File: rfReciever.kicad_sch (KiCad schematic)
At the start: 41 parts, among them J1 MOLEX 1054440001, J2 Conn_01x02, J3 Conn_01x02, J4 Conn_01x03, SW1 RF_RESET, SW2 RF_SLEEP, U1 TLV70130DBVR, U2 USBLC6-2SC6, U3 FT234XD-R, X1 DigiXBeeRX900Micro

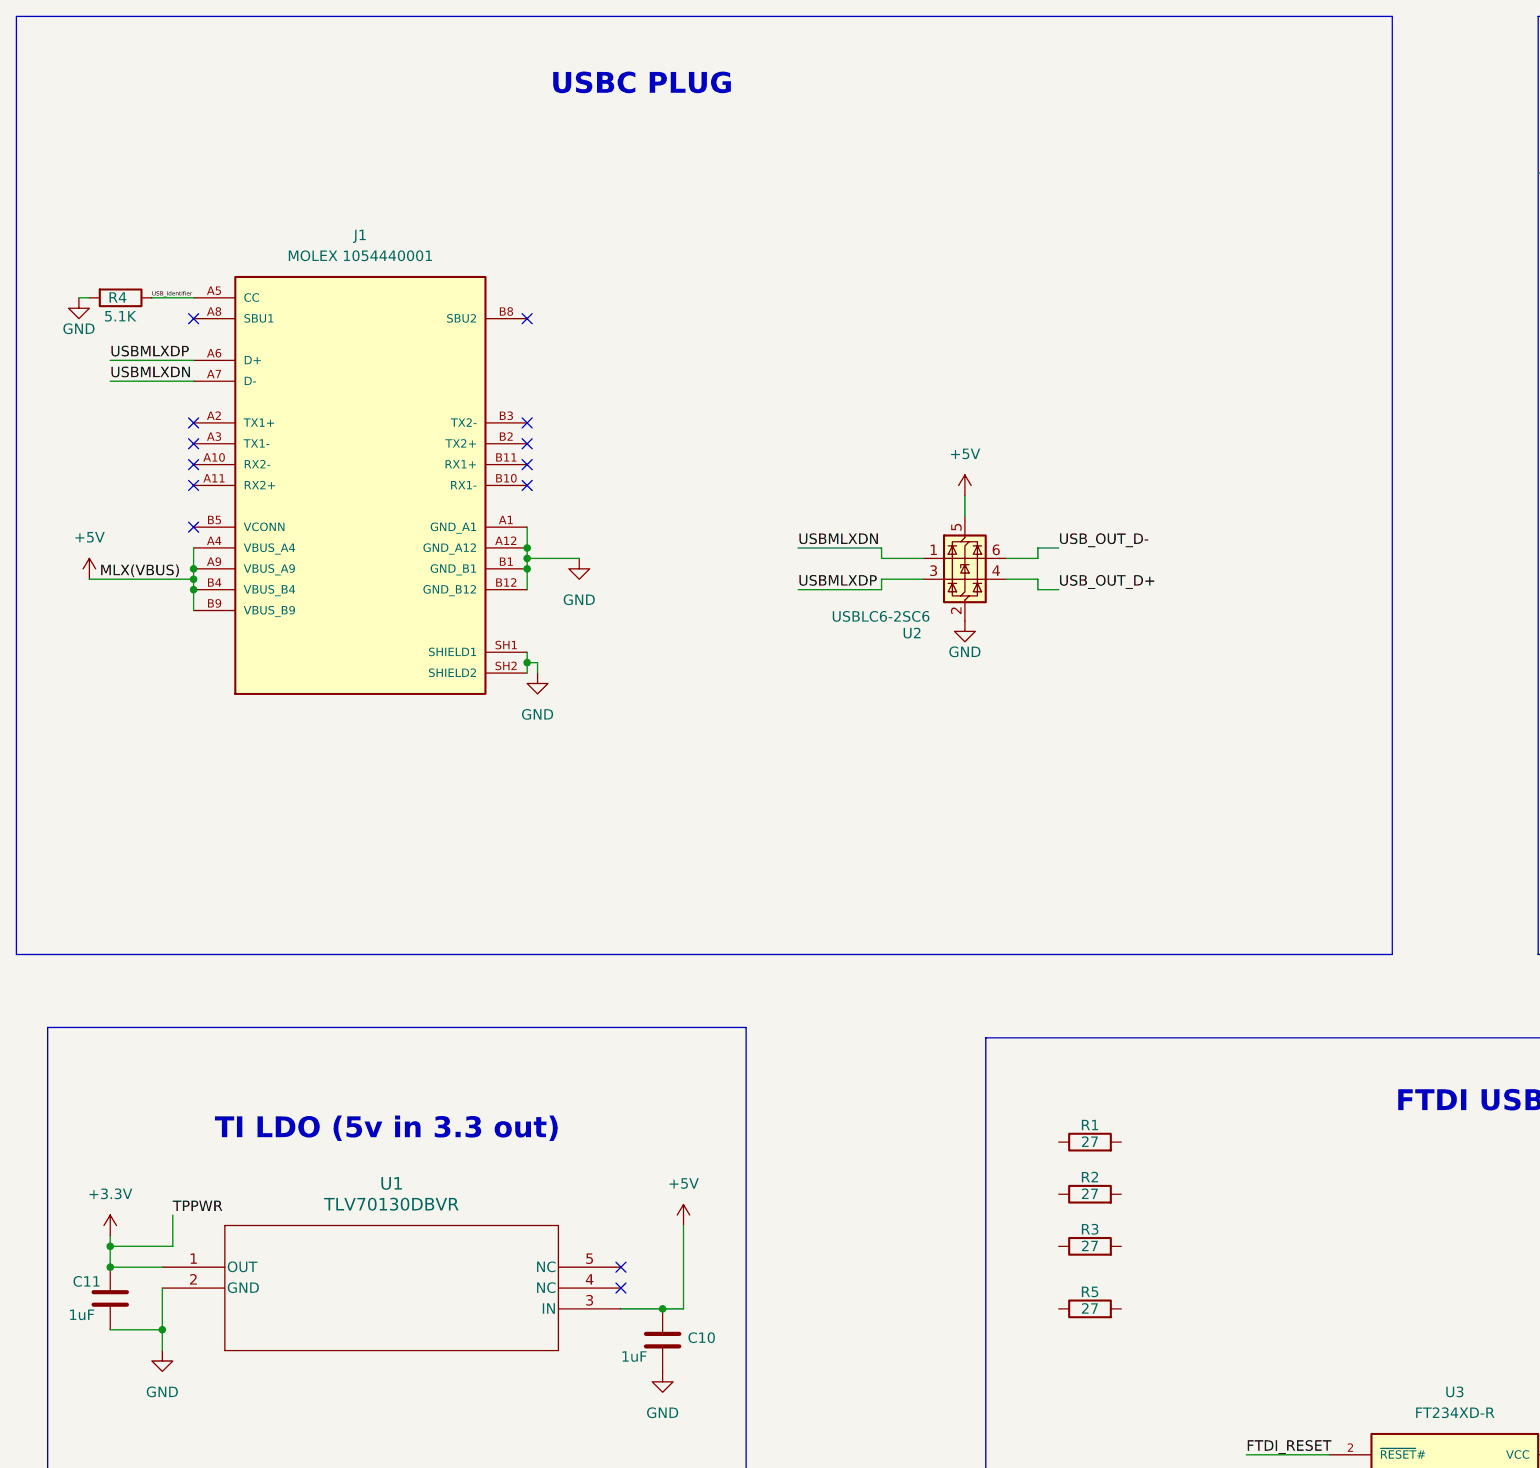
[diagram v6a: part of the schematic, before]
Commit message: More minor tweaks + silkscreen
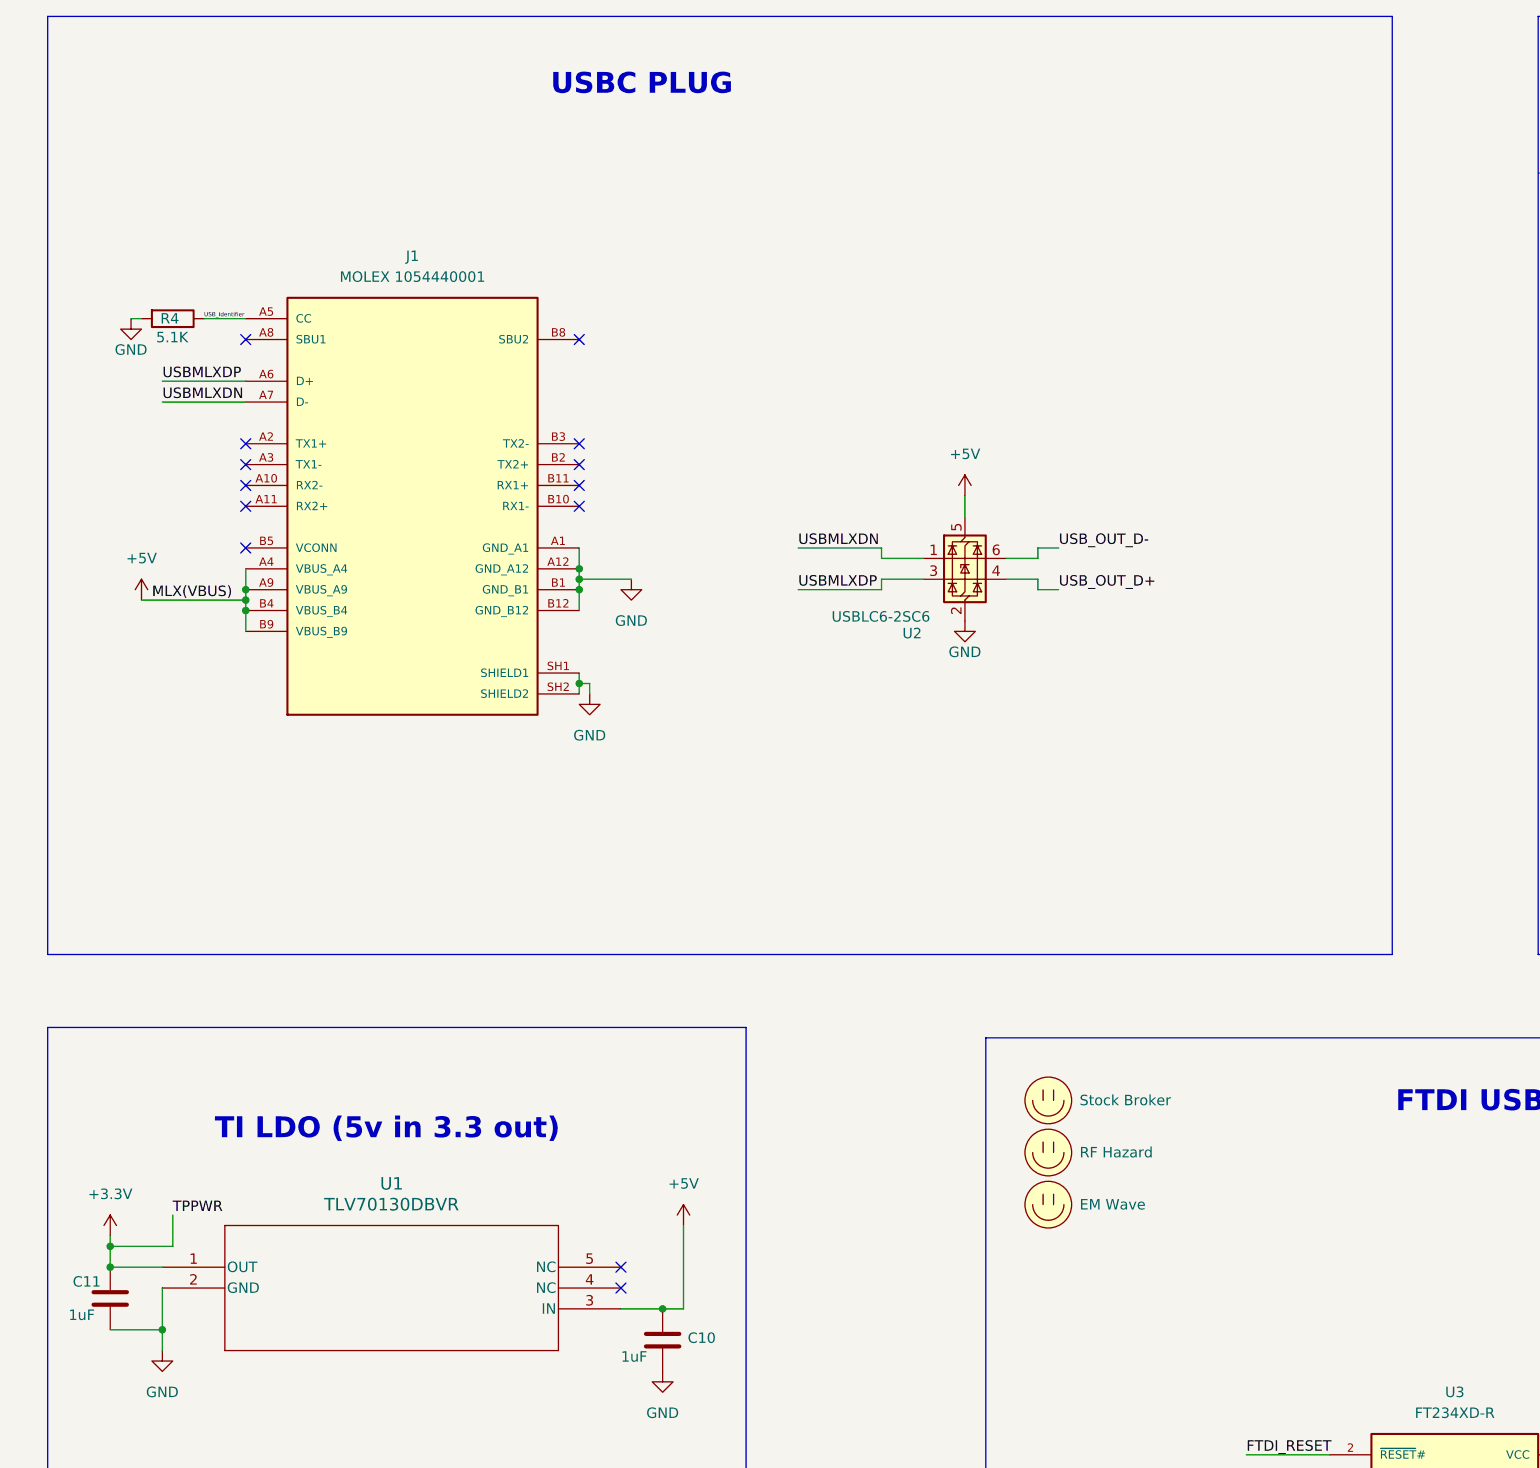
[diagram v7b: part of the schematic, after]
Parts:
- removed R1: 27, rfReciever-Footprints:stockBroker, symbol Device:R
- removed R2: 27, rfReciever-Footprints:RFHazard, symbol Device:R
- removed R3: 27, rfReciever-Footprints:dataNetwork, symbol Device:R
- removed R5: 27, rfReciever-Footprints:emWave, symbol Device:R
- added LOGO1: Stock Broker, rfReciever-Footprints:stockBroker, symbol utsvt-misc:Logo_Placeholder
- added LOGO2: RF Hazard, rfReciever-Footprints:RFHazard, symbol utsvt-misc:Logo_Placeholder
- added LOGO3: EM Wave, rfReciever-Footprints:emWave, symbol utsvt-misc:Logo_Placeholder
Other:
- moved on the sheet: J1, R4

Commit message: fixed drc
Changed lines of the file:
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@@
 (kicad_sch
-	(version 20231120)
+	(version 20250114)
 	(generator "eeschema")
-	(generator_version "8.0")
+	(generator_version "9.0")
 	(paper "A3")
+	(rectangle
+		(start 203.2 30.48)
+		(end 370.84 144.78)
+		(stroke
+			(width 0)
+			(type default)
+		)
+		(fill
+			(type none)
+		)
+	)
+	(rectangle
+		(start 299.72 167.64)
+		(end 382.27 213.36)
+		(stroke
+			(width 0)
+			(type default)
+		)
+		(fill
+			(type none)
+		)
+	)
+	(rectangle
+		(start 21.59 153.67)
+		(end 106.68 266.7)
+		(stroke
+			(width 0)
+			(type default)
+		)
+		(fill
+			(type none)
+		)
+	)
+	(rectangle
+		(start 135.89 154.94)
+		(end 267.97 267.97)
+		(stroke
+			(width 0)
+			(type default)
+		)
+		(fill
+			(type none)
+		)
+	)
+	(rectangle
+		(start 21.59 30.48)
+		(end 185.42 144.78)
+		(stroke
+			(width 0)
+			(type default)
+		)
+		(fill
+			(type none)
+		)
+	)
+	(text "FTDI USB-UART"
+		(exclude_from_sim no)
+		(at 200.914 162.814 0)
+		(effects
+			(font
+				(size 2.54 2.54)
+				(thickness 0.508)
+				(bold yes)
+			)
+		)
+	)
+	(text "Test Points, PWR, TX, RX"
+		(exclude_from_sim no)
+		(at 341.122 171.45 0)
+		(effects
+			(font
+				(size 2.54 2.54)
+				(thickness 0.508)
+				(bold yes)
+			)
+		)
+	)
+	(text "TI LDO (5v in 3.3 out)"
+		(exclude_from_sim no)
+		(at 62.992 166.116 0)
+		(effects
+			(font
+				(size 2.54 2.54)
+				(thickness 0.508)
+				(bold yes)
+			)
+		)
+	)
+	(text "XBeeRF MODULE MICRO"
+		(exclude_from_sim no)
+		(at 287.528 37.592 0)
+		(effects
+			(font
+				(size 2.54 2.54)
+				(thickness 0.508)
+				(bold yes)
+			)
+		)
+	)
+	(text "USBC PLUG"
+		(exclude_from_sim no)
+		(at 93.98 38.862 0)
+		(effects
+			(font
+				(size 2.54 2.54)
+				(thickness 0.508)
+				(bold yes)
+			)
+		)
+	)
 	(junction
 		(at 232.41 218.44)
@@
 		)
 	)
-	(rectangle
-		(start 203.2 30.48)
-		(end 370.84 144.78)
-		(stroke
-			(width 0)
-			(type default)
-		)
-		(fill
-			(type none)
-		)
-	)
-	(rectangle
-		(start 299.72 167.64)
-		(end 382.27 213.36)
-		(stroke
-			(width 0)
-			(type default)
-		)
-		(fill
-			(type none)
-		)
-	)
-	(rectangle
-		(start 21.59 153.67)
-		(end 106.68 266.7)
-		(stroke
-			(width 0)
-			(type default)
-		)
-		(fill
-			(type none)
-		)
-	)
-	(rectangle
-		(start 135.89 154.94)
-		(end 267.97 267.97)
-		(stroke
-			(width 0)
-			(type default)
-		)
-		(fill
-			(type none)
-		)
-	)
-	(rectangle
-		(start 21.59 30.48)
-		(end 185.42 144.78)
-		(stroke
-			(width 0)
-			(type default)
-		)
-		(fill
-			(type none)
-		)
-	)
-	(text "FTDI USB-UART"
-		(exclude_from_sim no)
-		(at 200.914 162.814 0)
-		(effects
-			(font
-				(size 2.54 2.54)
-				(thickness 0.508)
-				(bold yes)
-			)
-		)
-	)
-	(text "Test Points, PWR, TX, RX"
-		(exclude_from_sim no)
-		(at 341.122 171.45 0)
-		(effects
-			(font
-				(size 2.54 2.54)
-				(thickness 0.508)
-				(bold yes)
-			)
-		)
-	)
-	(text "TI LDO (5v in 3.3 out)"
-		(exclude_from_sim no)
-		(at 62.992 166.116 0)
-		(effects
-			(font
-				(size 2.54 2.54)
-				(thickness 0.508)
-				(bold yes)
-			)
-		)
-	)
-	(text "XBeeRF MODULE MICRO"
-		(exclude_from_sim no)
-		(at 287.528 37.592 0)
-		(effects
-			(font
-				(size 2.54 2.54)
-				(thickness 0.508)
-				(bold yes)
-			)
-		)
-	)
-	(text "USBC PLUG"
-		(exclude_from_sim no)
-		(at 93.98 38.862 0)
-		(effects
-			(font
-				(size 2.54 2.54)
-				(thickness 0.508)
-				(bold yes)
-			)
-		)
-	)
 	(label "USBDM"
 		(at 208.28 215.9 0)
-		(fields_autoplaced yes)
 		(effects
 			(font
@@
 	(label "RF_TXD"
 		(at 309.88 62.23 0)
-		(fields_autoplaced yes)
 		(effects
 			(font
@@
 	(label "RF_TXD"
 		(at 168.91 210.82 0)
-		(fields_autoplaced yes)
 		(effects
 			(font
@@
 	(label "RF_TXD"
 		(at 330.2 180.34 0)
-		(fields_autoplaced yes)
 		(effects
 			(font
@@
 	(label "UART_RTS"
 		(at 322.58 50.8 0)
-		(fields_autoplaced yes)
 		(effects
 			(font
@@
 	(label "RF_SW_SLEEP"
 		(at 356.87 106.68 90)
-		(fields_autoplaced yes)
 		(effects
 			(font
@@
 	(label "USB_Identifier"
 		(at 40.64 67.31 0)
-		(fields_autoplaced yes)
 		(effects
 			(font
@@
 	(label "RF_SLEEP"
 		(at 330.2 191.77 0)
-		(fields_autoplaced yes)
 		(effects
 			(font
@@
 	(label "USB_OUT_D+"
 		(at 144.78 100.33 0)
-		(fields_autoplaced yes)
 		(effects
 			(font
@@
 	(label "RF_D9"
 		(at 328.93 120.65 0)
-		(fields_autoplaced yes)
 		(effects
 			(font
@@
 	(label "FTDI_RESET"
 		(at 214.63 209.55 0)
-		(fields_autoplaced yes)
 		(effects
 			(font
@@
 	(label "UART_CTS"
 		(at 168.91 215.9 0)
-		(fields_autoplaced yes)
 		(effects
 			(font
@@
 	(label "USBMLXDP"
 		(at 35.56 74.93 0)
-		(fields_autoplaced yes)
 		(effects
 			(font
@@
 	(label "RF_PWM"
 		(at 304.8 113.03 0)
-		(fields_autoplaced yes)
 		(effects
 			(font
@@
 	(label "RF_SLEEP"
 		(at 332.74 106.68 0)
-		(fields_autoplaced yes)
 		(effects
 			(font
@@
 	(label "USB_OUT_D-"
 		(at 233.68 215.9 0)
-		(fields_autoplaced yes)
 		(effects
 			(font
@@
 	(label "UART_CTS"
 		(at 313.69 43.18 0)
-		(fields_autoplaced yes)
 		(effects
 			(font
@@
 	(label "USB_OUT_D-"
 		(at 144.78 95.25 0)
-		(fields_autoplaced yes)
 		(effects
 			(font
@@
 	(label "USBDP"
 		(at 208.28 218.44 0)
-		(fields_autoplaced yes)
 		(effects
 			(font
@@
 	(label "RF_RESET"
 		(at 330.2 189.23 0)
-		(fields_autoplaced yes)
 		(effects
 			(font
@@
 	(label "RF_RXD"
 		(at 330.2 182.88 0)
-		(fields_autoplaced yes)
 		(effects
 			(font
@@
 	(label "USB_OUT_D+"
 		(at 233.68 218.44 0)
-		(fields_autoplaced yes)
 		(effects
 			(font
@@
 	(label "RF_D7"
 		(at 308.61 123.19 0)
-		(fields_autoplaced yes)
 		(effects
 			(font
@@
 	(label "RF_RESET"
 		(at 318.77 80.01 0)
-		(fields_autoplaced yes)
 		(effects
 			(font
@@
 	(label "FTDI_RESET"
 		(at 167.64 205.74 0)
-		(fields_autoplaced yes)
 		(effects
 			(font
@@
 	(label "TPPWR"
 		(at 36.83 176.53 0)
-		(fields_autoplaced yes)
 		(effects
 			(font
@@
 	(label "RF_SW_RESET"
 		(at 347.98 80.01 0)
-		(fields_autoplaced yes)
 		(effects
 			(font
@@
 	(label "RF_RXD"
 		(at 309.88 66.04 0)
-		(fields_autoplaced yes)
 		(effects
 			(font
@@
 	(label "RF_SLEEP"
 		(at 318.77 76.2 0)
-		(fields_autoplaced yes)
 		(effects
 			(font
@@
 	(label "RF_BOOTMODE"
 		(at 309.88 72.39 0)
-		(fields_autoplaced yes)
 		(effects
 			(font
@@
 	(label "MLX(VBUS)"
 		(at 34.29 101.6 0)
-		(fields_autoplaced yes)
 		(effects
 			(font
@@
 	(label "RF_DSLEEP"
 		(at 306.07 102.87 0)
-		(fields_autoplaced yes)
 		(effects
 			(font
@@
 	(label "USBMLXDN"
 		(at 113.03 95.25 0)
-		(fields_autoplaced yes)
 		(effects
 			(font
@@
 	(label "USBMLXDN"
 		(at 35.56 77.47 0)
-		(fields_autoplaced yes)
 		(effects
 			(font
@@
 	(label "USBMLXDP"
 		(at 113.03 100.33 0)
-		(fields_autoplaced yes)
 		(effects
 			(font
@@
 	(label "RF_D8"
 		(at 318.77 120.65 0)
-		(fields_autoplaced yes)
 		(effects
 			(font
@@
 	(label "RF_ASSOCIATE"
 		(at 314.96 99.06 0)
-		(fields_autoplaced yes)
 		(effects
 			(font
@@
 	(label "RF_RXD"
 		(at 168.91 213.36 0)
-		(fields_autoplaced yes)
 		(effects
 			(font
@@
 	(label "UART_RTS"
 		(at 168.91 218.44 0)
-		(fields_autoplaced yes)
 		(effects
 			(font
@@
 		)
 	)
+	(embedded_fonts no)
 )
